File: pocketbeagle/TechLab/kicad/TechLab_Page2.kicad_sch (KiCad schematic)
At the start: 50 parts, among them J2 USB_C_Receptacle_USB2.0, T1 3904, T2 EAALSTIC1708A0, U5 MCP23S18-E/MJ, U6 FT230XQ-R, U7 SN74LV4053A

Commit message: TechLab: more cleanup
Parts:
- BUZZER0: Field7 (none) -> BUZZER
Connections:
- net GND: no longer J2.A12 (GND), J2.B1 (GND), J2.B12 (GND)
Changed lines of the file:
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@@
 		)
 		(instances
-			(project "TechLab"
+			(project ""
+				(path "/199e843b-8c9a-4ca8-a6e6-fde18a374d00/288abbbe-f51f-4467-a9d7-89cdf05e44f0"
+					(reference "J2")
+					(unit 1)
+				)
 				(path "/199e843b-8c9a-4ca8-a6e6-fde18a374d00/4dffbcbf-91b6-4a9c-9fc6-f872a45552ad"
 					(reference "J2")
@@
 				)
 				(justify left bottom)
+				(hide yes)
 			)
 		)
@@
 			)
 		)
+		(property "Field7" "BUZZER"
+			(at 55.88 179.832 0)
+			(effects
+				(font
+					(size 1.27 1.27)
+				)
+			)
+		)

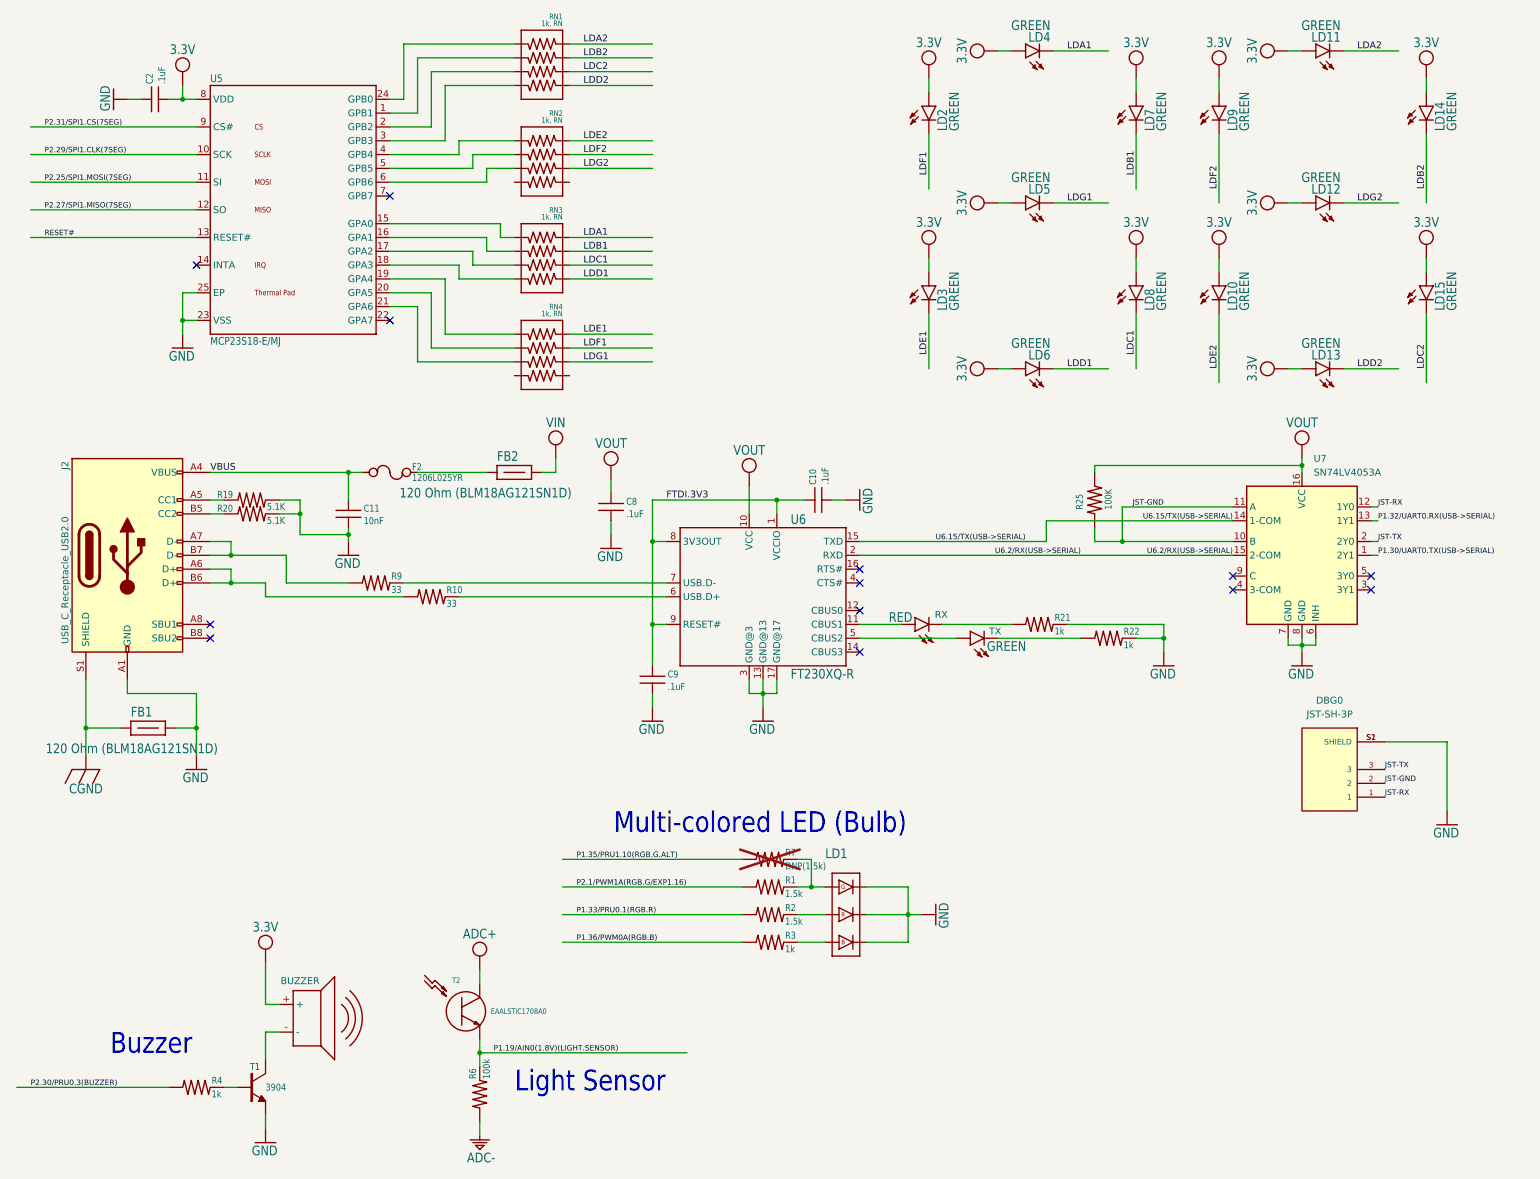
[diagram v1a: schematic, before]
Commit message: TechLab: fix most ERCs
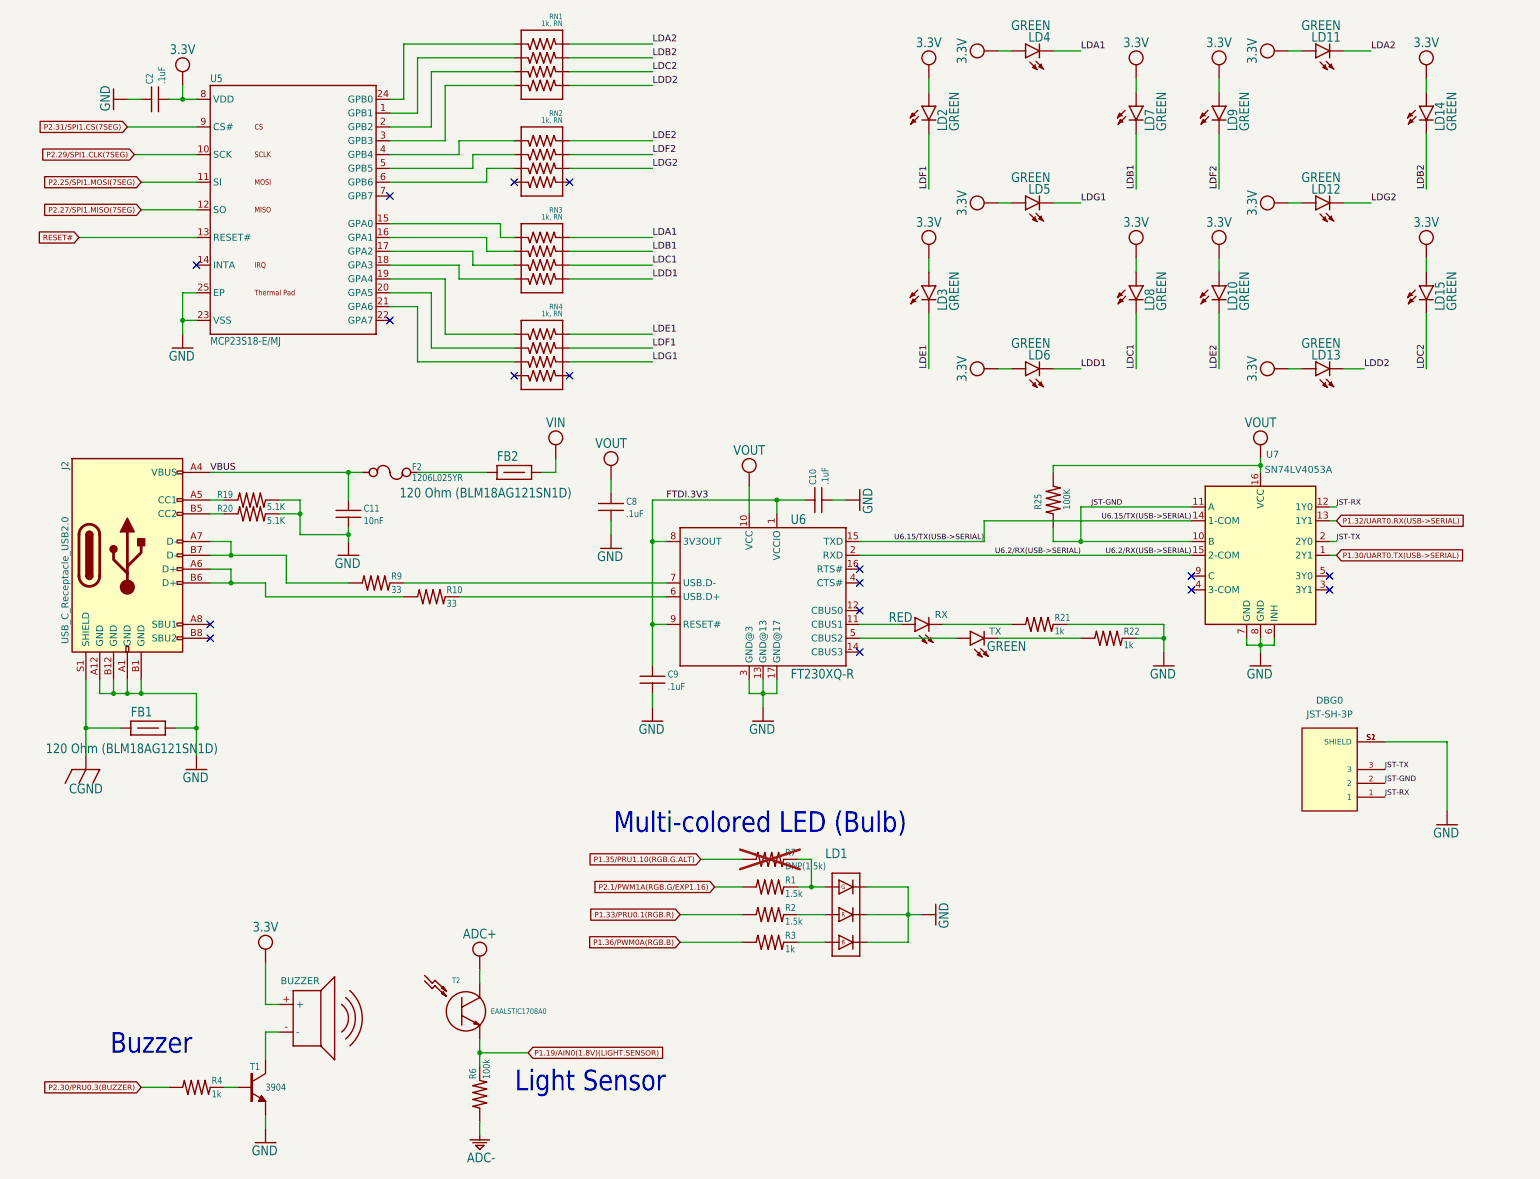
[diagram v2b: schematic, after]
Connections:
- net GND: now also J2.A12 (GND), J2.B1 (GND), J2.B12 (GND)
- net P1.19/AIN0(1.8V)(LIGHT.SENSOR) renamed P1.19/AIN0(1.8V)(LIGHT.SENSOR)
- net P1.30/UART0.TX(USB->SERIAL) renamed P1.30/UART0.TX(USB->SERIAL)
- net P1.32/UART0.RX(USB->SERIAL) renamed P1.32/UART0.RX(USB->SERIAL)
- net P1.33/PRU0.1(RGB.R) renamed P1.33/PRU0.1(RGB.R)
- net P1.35/PRU1.10(RGB.G.ALT) renamed P1.35/PRU1.10(RGB.G.ALT)
- net P1.36/PWM0A(RGB.B) renamed P1.36/PWM0A(RGB.B)
- net P2.1/PWM1A(RGB.G/EXP1.16) renamed P2.1/PWM1A(RGB.G/EXP1.16)
- net P2.25/SPI1.MOSI(7SEG) renamed P2.25/SPI1.MOSI(7SEG)
- net P2.27/SPI1.MISO(7SEG) renamed P2.27/SPI1.MISO(7SEG)
- net P2.29/SPI1.CLK(7SEG) renamed P2.29/SPI1.CLK(7SEG)
- net P2.30/PRU0.3(BUZZER) renamed P2.30/PRU0.3(BUZZER)
- net P2.31/SPI1.CS(7SEG) renamed P2.31/SPI1.CS(7SEG)
- no-connect marks 13 -> 17
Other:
- moved on the sheet: R25, U7

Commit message: TechLab: ideas for replacements to buzzer and light sensor
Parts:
- BUZZER0: MANUFACTURER Yongyin Elec -> CUI Devices; MPN SMD-140035H-05027 -> CSS-H5B43-SMT-TR
- T2: MANUFACTURER Everlight -> Inolux; MPN EAALSTIC1708A0 -> IN-S63DTLS
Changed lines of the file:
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@@
 			)
 		)
-		(property "MANUFACTURER" "Everlight"
+		(property "MANUFACTURER" "Inolux"
 			(at 86.36 185.42 0)
 			(effects
@@
 			)
 		)
-		(property "MPN" "EAALSTIC1708A0"
+		(property "MPN" "IN-S63DTLS"
 			(at 86.36 185.42 0)
 			(effects
@@
 			)
 		)
-		(property "MANUFACTURER" "Yongyin Elec"
+		(property "MANUFACTURER" "CUI Devices"
 			(at 57.15 186.69 0)
 			(effects
@@
 			)
 		)
-		(property "MPN" "SMD-140035H-05027"
+		(property "MPN" "CSS-H5B43-SMT-TR"
 			(at 57.15 186.69 0)
 			(effects

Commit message: TechLab: alternate buzzer
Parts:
- BUZZER0: MANUFACTURER CUI Devices -> PUI Audio; MPN CSS-H5B43-SMT-TR -> SMT-1427-S-5V-HT-R
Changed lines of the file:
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@@
 			)
 		)
-		(property "MANUFACTURER" "CUI Devices"
+		(property "MANUFACTURER" "PUI Audio"
 			(at 57.15 186.69 0)
 			(effects
@@
 			)
 		)
-		(property "MPN" "CSS-H5B43-SMT-TR"
+		(property "MPN" "SMT-1427-S-5V-HT-R"
 			(at 57.15 186.69 0)
 			(effects
